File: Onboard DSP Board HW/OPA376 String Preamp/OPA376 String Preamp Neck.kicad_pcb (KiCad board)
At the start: 2 copper layers, 28.4 x 89.9 mm, 48 parts, among them J1 Input, J10 Input, J14 Input, J5 Input, U1 TLV9001IDCK, U2 TLV9001IDCK, U3 TLV9001IDCK, U4 TLV9001IDCK

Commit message: WIP
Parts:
- C1, C11, C13, C15: footprint Capacitor_SMD:C_0402_1005Metric -> Capacitor_SMD:C_0603_1608Metric
- C2: value C -> 10uF; footprint Capacitor_SMD:C_0402_1005Metric -> Capacitor_SMD:C_0603_1608Metric
- R1: value R -> 100K
- R2: value R -> 43K
- U1, U2, U3, U4: value TLV9001IDCK -> OPA376
- moved C2 3.24 mm to (106.7, 60.6), turned to 180 degrees
- moved R1 1.31 mm to (107.2, 58.1), turned to 0 degrees
- moved C15 1.08 mm to (96.5, 126.7), turned to 0 degrees
- moved C13 1.07 mm to (96.5, 109.4), turned to 0 degrees
- moved C1 0.99 mm to (96.6, 75.2), turned to 0 degrees
- moved C11 0.98 mm to (96.6, 92.0), turned to 0 degrees
- moved R2 0.82 mm to (107.2, 59.2), turned to 180 degrees
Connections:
- C2 pad 1: /SIngle FET preamp/3.3V -> /SIngle FET preamp/MidRail
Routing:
- net GND: track 16.4 -> 9.89 mm
- net /SIngle FET preamp/3.3V: track 101.2 -> 96.9 mm
- net /SIngle FET preamp/MidRail: track 76.8 -> 77.9 mm
- net Net-(C15-Pad2): track 1.11 -> 1.70 mm
- net Net-(C13-Pad2): track 1.11 -> 1.68 mm
- net Net-(C11-Pad2): track 1.11 -> 1.62 mm

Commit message: WIP
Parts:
- moved R1 42.3 mm to (101.6, 100.0), turned to 90 degrees
- moved R2 41.1 mm to (102.7, 100.0), turned to -90 degrees
- moved C2 39.9 mm to (100.2, 100.0), turned to -90 degrees
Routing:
- net /SIngle FET preamp/MidRail: track 77.9 -> 82.5 mm
- net /SIngle FET preamp/3.3V: track 96.9 -> 97.8 mm, vias 4 -> 5
- net GND: vias 29 -> 27

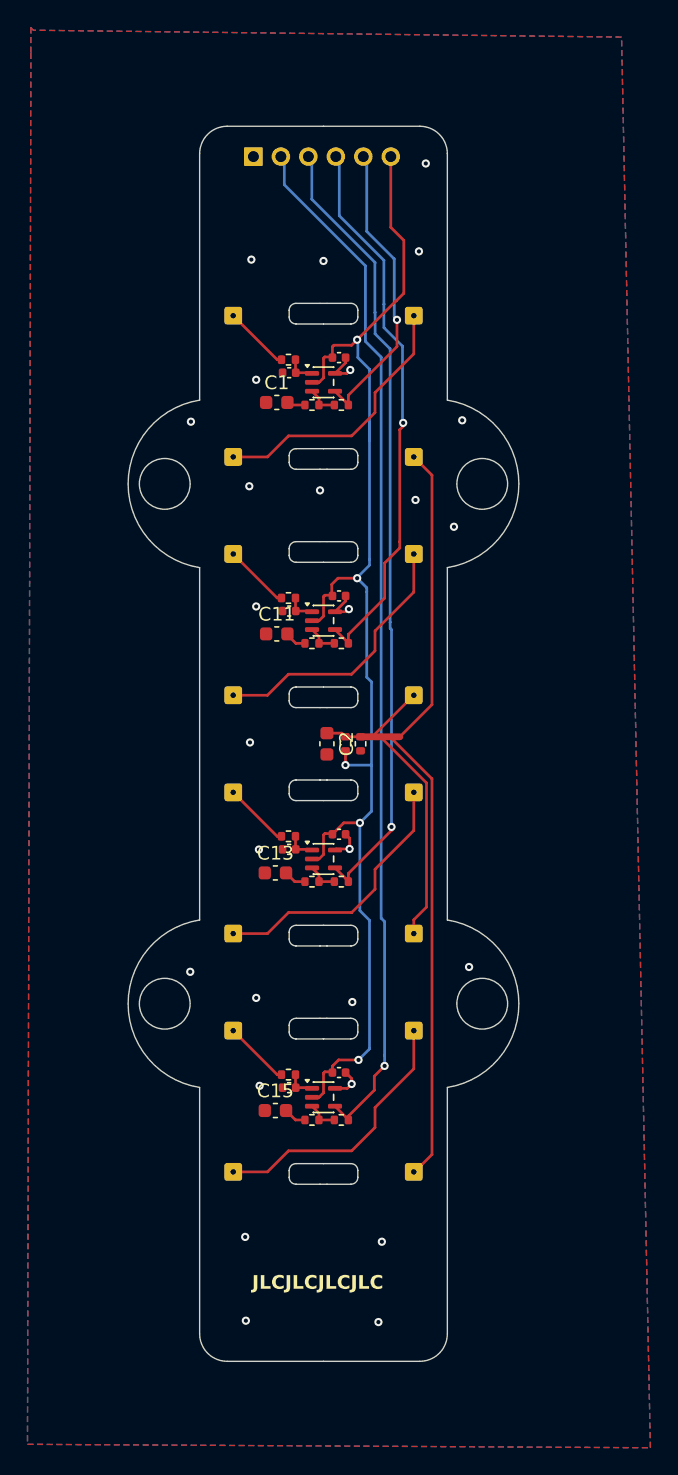
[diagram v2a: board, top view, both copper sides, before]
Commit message: Fix Opamp supplies, simulate, add safety resistor to V+
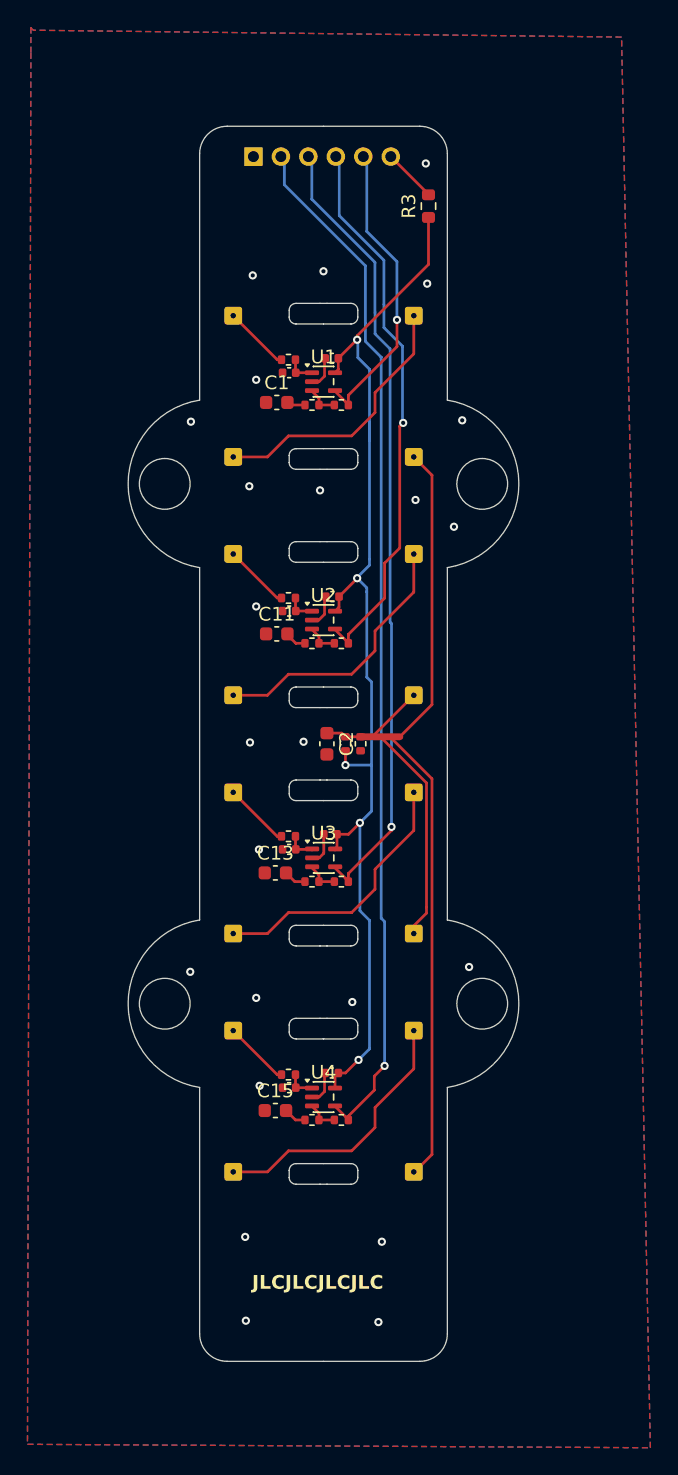
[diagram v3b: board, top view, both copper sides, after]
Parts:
- added R3: 47, Resistor_SMD:R_0603_1608Metric, F.Cu at (107.6, 60.9)
- U1, U2, U3, U4: value OPA376 -> OPA376xxDCK
- moved C19 0.63 mm to (100.5, 106.6), turned to 180 degrees
- moved C17 0.53 mm to (100.6, 71.9), turned to 180 degrees
- moved C20 0.53 mm to (100.6, 124.0), turned to 180 degrees
- moved C18 0.48 mm to (100.7, 89.3), turned to 180 degrees
- moved U3 0.08 mm to (100.0, 108.3)
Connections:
- net Net-(J1-Pin_1) renamed /Input
- net Net-(J10-Pin_1) renamed /SIngle FET preamp2/Input
- net Net-(J14-Pin_1) renamed /SIngle FET preamp3/Input
- net Net-(J5-Pin_1) renamed /SIngle FET preamp1/Input
- J9 pad 6: /SIngle FET preamp/3.3V -> Net-(J9-Pin_6)
- U1 pad 2: /SIngle FET preamp/3.3V -> GND
- U1 pad 5: GND -> /SIngle FET preamp/3.3V
- U2 pad 2: /SIngle FET preamp/3.3V -> GND
- U2 pad 5: GND -> /SIngle FET preamp/3.3V
- U3 pad 2: /SIngle FET preamp/3.3V -> GND
- U3 pad 5: GND -> /SIngle FET preamp/3.3V
- U4 pad 2: /SIngle FET preamp/3.3V -> GND
- U4 pad 5: GND -> /SIngle FET preamp/3.3V
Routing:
- net /SIngle FET preamp/3.3V: track 97.8 -> 82.5 mm
- net Net-(J9-Pin_6): track 0.00 -> 4.07 mm
- net /SIngle FET preamp/MidRail: track 82.5 -> 82.0 mm
- net GND: track 9.89 -> 9.63 mm, vias 27 -> 22
- net (no net): vias 0 -> 2

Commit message: WIP
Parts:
- U1, U2, U3, U4: value OPA376xxDCK -> OPA376AIDCKT
- moved J9 1.05 mm to (94.9, 58.3)
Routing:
- net /SIngle FET preamp3/Output: track 75.8 -> 74.7 mm
- net /SIngle FET preamp1/Output: track 40.5 -> 39.5 mm
- net /SIngle FET preamp/Output: track 22.0 -> 20.9 mm
- net /SIngle FET preamp2/Output: track 58.0 -> 56.9 mm
- net GND: vias 22 -> 24
- net (no net): vias 2 -> 0

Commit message: WIP
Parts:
- removed C2: 10uF, Capacitor_SMD:C_0603_1608Metric
- removed J9: ~, Connector_PinHeader_2.00mm:PinHeader_1x06_P2.00mm_Horizontal
- removed R1: 100K, Resistor_SMD:R_0402_1005Metric
- added C21: 220pF, Capacitor_SMD:C_0402_1005Metric, F.Cu at (101.5, 128.5)
- added C3: 100nF, Capacitor_SMD:C_0603_1608Metric, F.Cu at (107.7, 64.6)
- added J18: ~, Connector_PinHeader_2.00mm:PinHeader_1x07_P2.00mm_Horizontal, B.Cu at (93.8, 57.7)
- added R25: 27K, Resistor_SMD:R_0402_1005Metric, F.Cu at (97.4, 74.0)
- added R26: 27K, Resistor_SMD:R_0402_1005Metric, F.Cu at (97.5, 91.4)
- added R27: 27K, Resistor_SMD:R_0402_1005Metric, F.Cu at (97.4, 108.8)
- added R28: 27K, Resistor_SMD:R_0402_1005Metric, F.Cu at (97.5, 126.1)
- added U5: OPA376AIDCKR, Package_TO_SOT_SMD:SOT-353_SC-70-5, F.Cu at (101.3, 100.0)
- C1: value 22uF -> 100pF; footprint Capacitor_SMD:C_0603_1608Metric -> Capacitor_SMD:C_0402_1005Metric
- C11, C13, C15: value 22uF -> 220pF; footprint Capacitor_SMD:C_0603_1608Metric -> Capacitor_SMD:C_0402_1005Metric
- R2: value 43K -> 1K
- U1, U2, U3, U4: value OPA376AIDCKT -> OPA376AIDCKR
- moved C1 24.6 mm to (99.2, 99.6), turned to -90 degrees
- moved C11 16.3 mm to (100.8, 76.3), turned to 180 degrees
- moved C13 16.2 mm to (100.8, 93.8), turned to 180 degrees
- moved C15 16.2 mm to (101.0, 111.2), turned to 180 degrees
- moved R2 4.67 mm to (98.0, 99.6), turned to 90 degrees
- moved R3 0.35 mm to (107.7, 61.2), turned to -90 degrees
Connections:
- net /Input renamed /SIngle FET preamp/in
- net /SIngle FET preamp1/Input renamed /SIngle FET preamp1/in
- net /SIngle FET preamp2/Input renamed /SIngle FET preamp2/in
- net /SIngle FET preamp3/Input renamed /SIngle FET preamp3/in
- C1 pad 1: GND -> Net-(U5-+)
- C1 pad 2: Net-(C1-Pad2) -> GND
- C11 pad 1: GND -> /SIngle FET preamp/Output
- C11 pad 2: Net-(C11-Pad2) -> Net-(U1--)
- C13 pad 1: GND -> /SIngle FET preamp1/Output
- C13 pad 2: Net-(C13-Pad2) -> Net-(U2--)
- C15 pad 1: GND -> /SIngle FET preamp2/Output
- C15 pad 2: Net-(C15-Pad2) -> Net-(U3--)
- R14 pad 1: Net-(C1-Pad2) -> /SIngle FET preamp/MidRail
- R17 pad 1: Net-(C11-Pad2) -> /SIngle FET preamp/MidRail
- R2 pad 1: /SIngle FET preamp/MidRail -> /Bias
- R2 pad 2: GND -> Net-(U5-+)
- R20 pad 1: Net-(C13-Pad2) -> /SIngle FET preamp/MidRail
- R23 pad 1: Net-(C15-Pad2) -> /SIngle FET preamp/MidRail
- R3 pad 1: /SIngle FET preamp/3.3V -> /3V3
- R3 pad 2: Net-(J9-Pin_6) -> /SIngle FET preamp/3.3V
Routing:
- net /SIngle FET preamp/MidRail: track 82.0 -> 131.5 mm, vias 0 -> 8
- net /Bias: track 0.00 -> 49.2 mm, vias 0 -> 1
- net /3V3: track 0.00 -> 10.9 mm
- net Net-(J9-Pin_6): track 3.69 -> 0.00 mm
- net GND: track 9.63 -> 12.4 mm, vias 24 -> 32
- net Net-(U5-+): track 0.00 -> 2.55 mm
- net /SIngle FET preamp/3.3V: track 82.5 -> 80.8 mm
- net Net-(C15-Pad2): track 1.70 -> 0.00 mm
- net Net-(C13-Pad2): track 1.68 -> 0.00 mm
- net Net-(C11-Pad2): track 1.62 -> 0.00 mm
- net /SIngle FET preamp/Output: track 20.9 -> 22.5 mm
- net Net-(C1-Pad2): track 1.40 -> 0.00 mm
- net Net-(U2--): track 2.33 -> 3.64 mm
- net Net-(U3--): track 2.33 -> 3.54 mm
- net Net-(U4--): track 2.33 -> 3.52 mm
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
